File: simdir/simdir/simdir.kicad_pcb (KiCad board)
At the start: 2 copper layers, 5 parts, among them U2 MASWSS0178, U3 MASWSS0178, U4 MASWSS0178, U5 MASWSS0178, U6 MASWSS0178

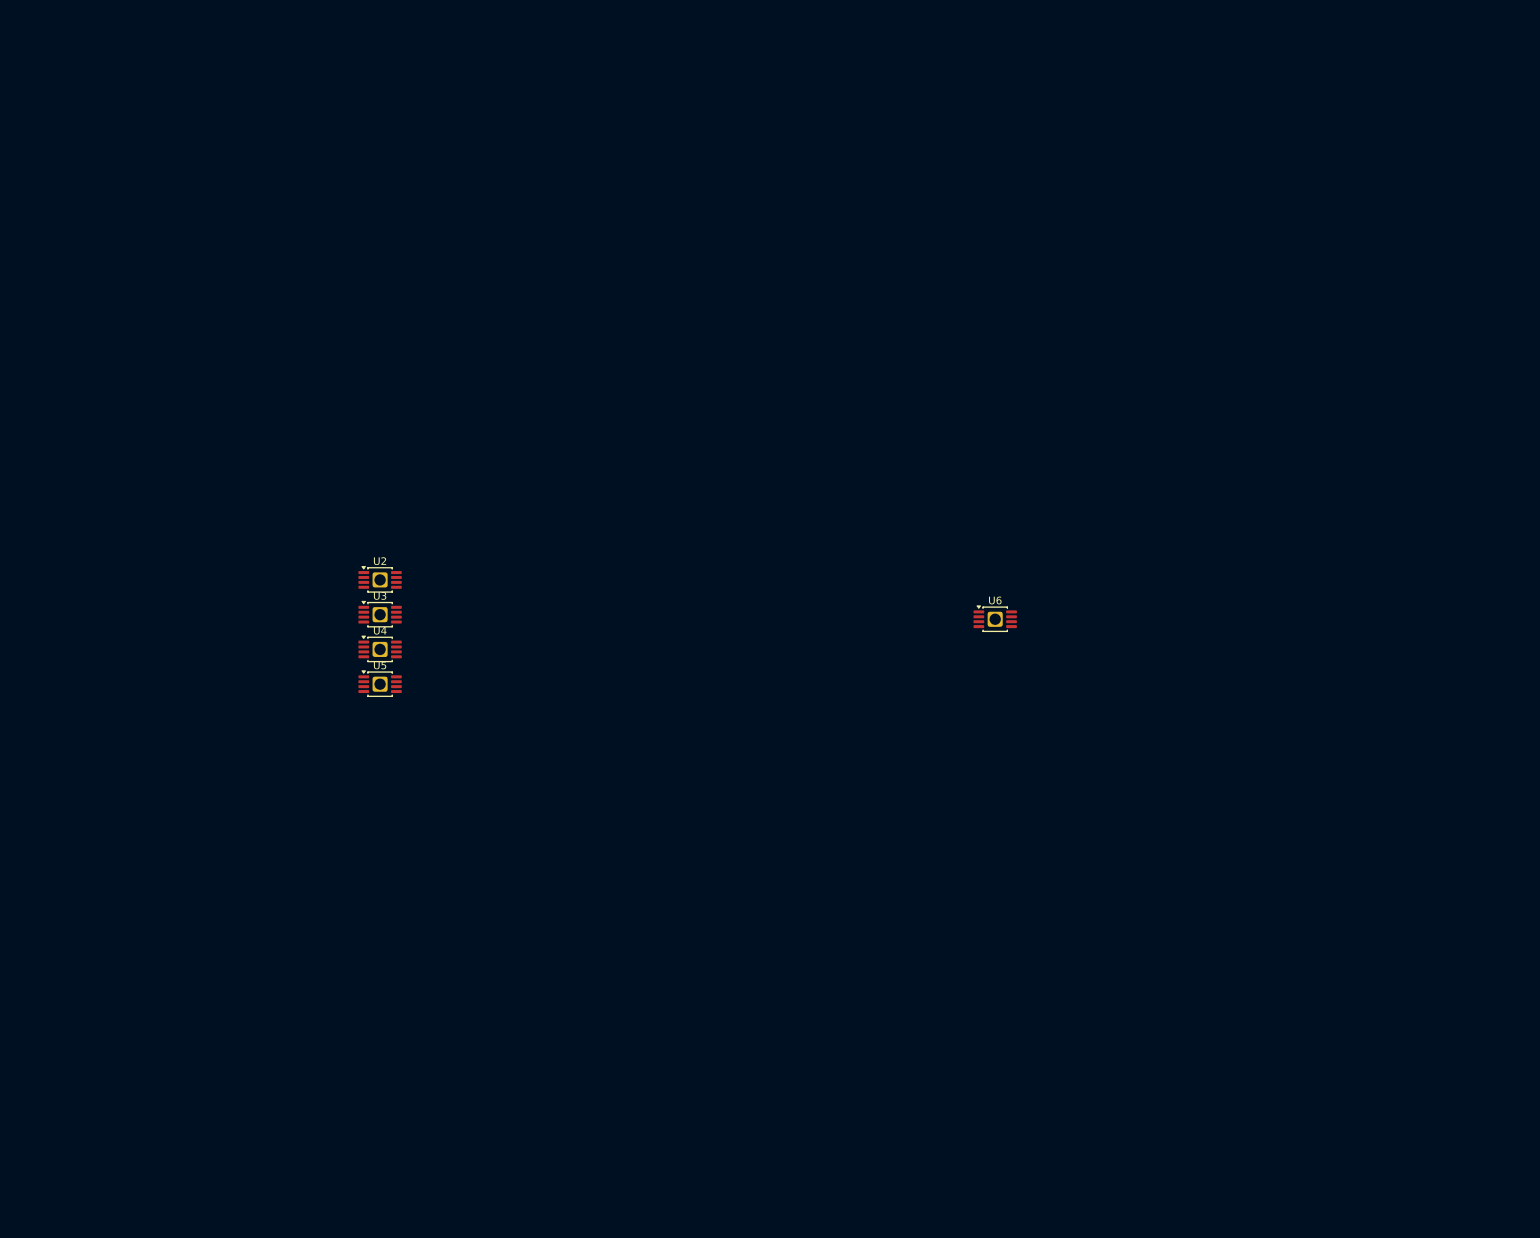
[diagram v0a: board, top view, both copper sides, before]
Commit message: Added channel block.
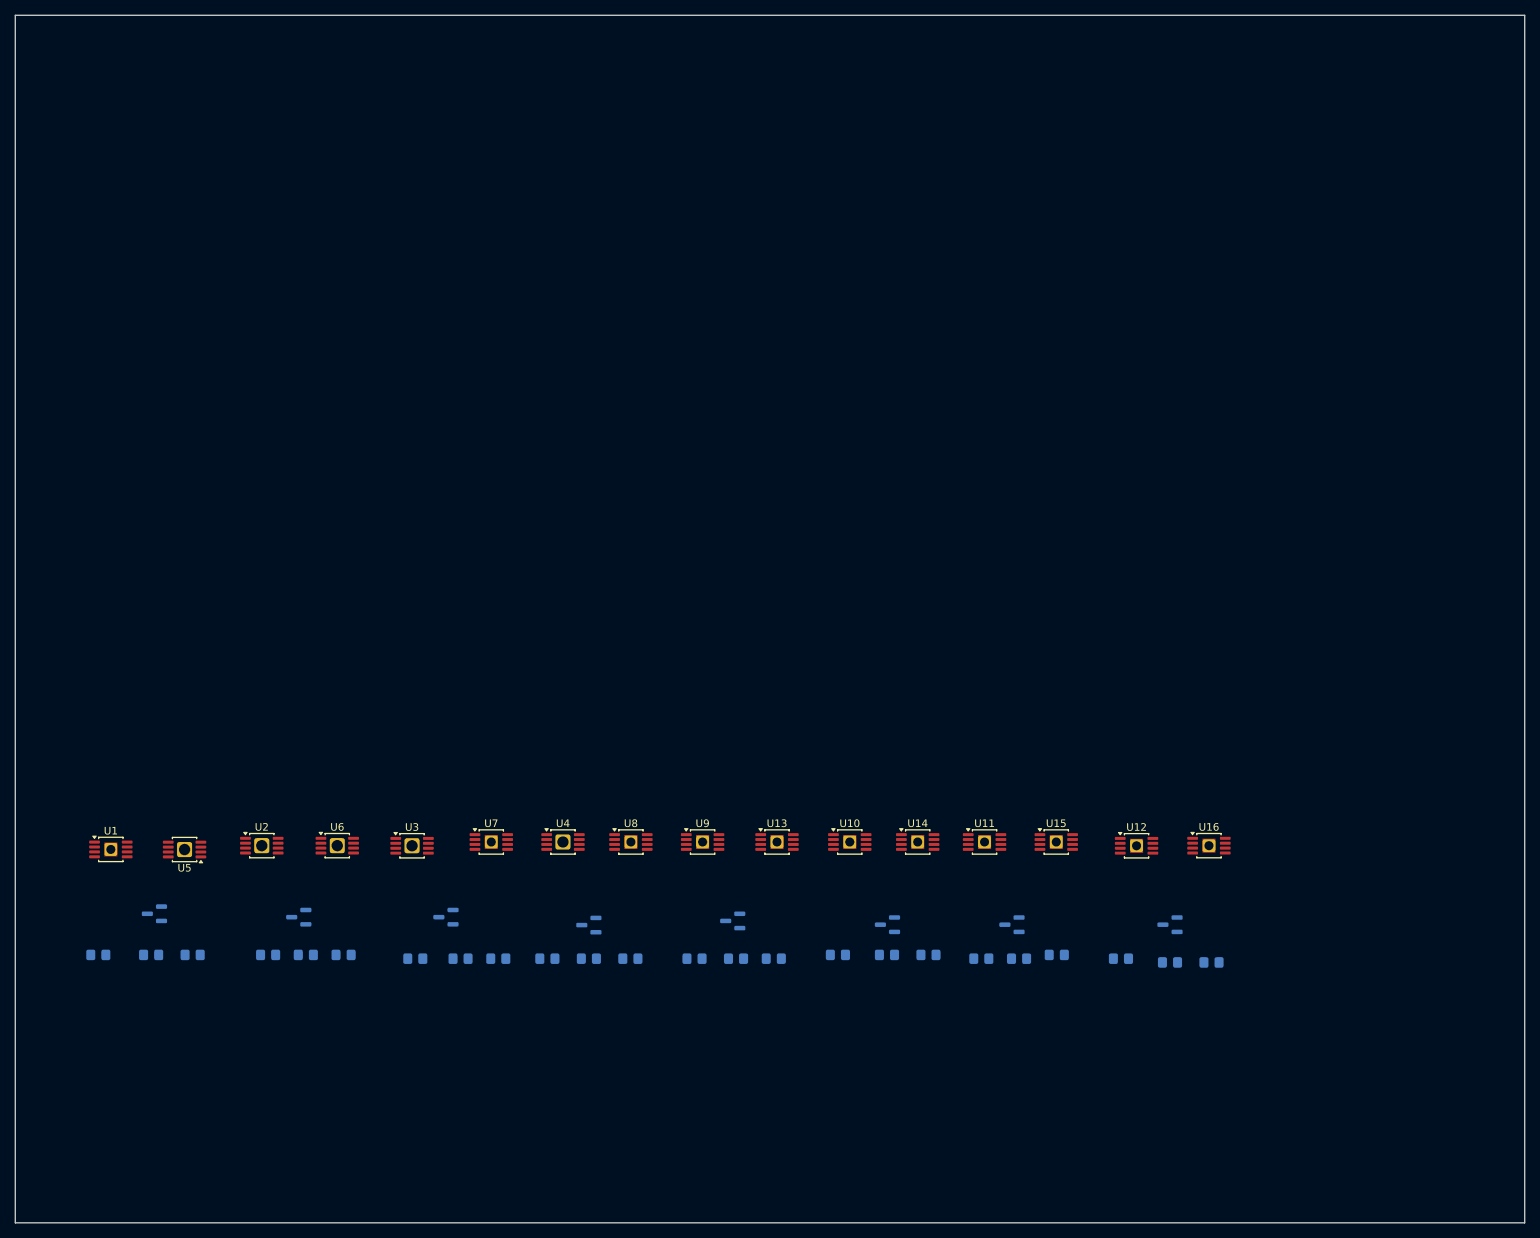
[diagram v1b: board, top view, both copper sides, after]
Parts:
- added Q1: BC847, Package_TO_SOT_SMD:SOT-23, B.Cu at (38.4, 139.1)
- added Q2: BC847, Package_TO_SOT_SMD:SOT-23, B.Cu at (57.6, 139.5)
- added Q3: BC847, Package_TO_SOT_SMD:SOT-23, B.Cu at (77.1, 139.5)
- added Q4: BC847, Package_TO_SOT_SMD:SOT-23, B.Cu at (96.0, 140.6)
- added Q5: BC847, Package_TO_SOT_SMD:SOT-23, B.Cu at (115.1, 140.0)
- added Q6: BC847, Package_TO_SOT_SMD:SOT-23, B.Cu at (135.6, 140.5)
- added Q7: BC847, Package_TO_SOT_SMD:SOT-23, B.Cu at (152.1, 140.5)
- added Q8: BC847, Package_TO_SOT_SMD:SOT-23, B.Cu at (173.0, 140.5)
- added R1: 10k, Resistor_SMD:R_0805_2012Metric_Pad1.20x1.40mm_HandSolder, B.Cu at (31.0, 144.5)
- added R10: 10k, Resistor_SMD:R_0805_2012Metric_Pad1.20x1.40mm_HandSolder, B.Cu at (90.5, 145.0)
- added R11: 4.7k, Resistor_SMD:R_0805_2012Metric_Pad1.20x1.40mm_HandSolder, B.Cu at (96.0, 145.0)
- added R12: 10k, Resistor_SMD:R_0805_2012Metric_Pad1.20x1.40mm_HandSolder, B.Cu at (101.5, 145.0)
- added R13: 10k, Resistor_SMD:R_0805_2012Metric_Pad1.20x1.40mm_HandSolder, B.Cu at (110.0, 145.0)
- added R14: 4.7k, Resistor_SMD:R_0805_2012Metric_Pad1.20x1.40mm_HandSolder, B.Cu at (115.5, 145.0)
- added R15: 10k, Resistor_SMD:R_0805_2012Metric_Pad1.20x1.40mm_HandSolder, B.Cu at (120.5, 145.0)
- added R16: 10k, Resistor_SMD:R_0805_2012Metric_Pad1.20x1.40mm_HandSolder, B.Cu at (129.0, 144.5)
- added R17: 4.7k, Resistor_SMD:R_0805_2012Metric_Pad1.20x1.40mm_HandSolder, B.Cu at (135.5, 144.5)
- added R18: 10k, Resistor_SMD:R_0805_2012Metric_Pad1.20x1.40mm_HandSolder, B.Cu at (141.0, 144.5)
- added R19: 10k, Resistor_SMD:R_0805_2012Metric_Pad1.20x1.40mm_HandSolder, B.Cu at (148.0, 145.0)
- added R2: 10k, Resistor_SMD:R_0805_2012Metric_Pad1.20x1.40mm_HandSolder, B.Cu at (38.0, 144.5)
- added R20: 4.7k, Resistor_SMD:R_0805_2012Metric_Pad1.20x1.40mm_HandSolder, B.Cu at (153.0, 145.0)
- added R21: 10k, Resistor_SMD:R_0805_2012Metric_Pad1.20x1.40mm_HandSolder, B.Cu at (158.0, 144.5)
- added R22: 10k, Resistor_SMD:R_0805_2012Metric_Pad1.20x1.40mm_HandSolder, B.Cu at (166.5, 145.0)
- added R23: 4.7k, Resistor_SMD:R_0805_2012Metric_Pad1.20x1.40mm_HandSolder, B.Cu at (173.0, 145.5)
- added R24: 10k, Resistor_SMD:R_0805_2012Metric_Pad1.20x1.40mm_HandSolder, B.Cu at (178.5, 145.5)
- added R3: 4.7k, Resistor_SMD:R_0805_2012Metric_Pad1.20x1.40mm_HandSolder, B.Cu at (43.5, 144.5)
- added R4: 10k, Resistor_SMD:R_0805_2012Metric_Pad1.20x1.40mm_HandSolder, B.Cu at (53.5, 144.5)
- added R5: 4.7k, Resistor_SMD:R_0805_2012Metric_Pad1.20x1.40mm_HandSolder, B.Cu at (58.5, 144.5)
- added R6: 10k, Resistor_SMD:R_0805_2012Metric_Pad1.20x1.40mm_HandSolder, B.Cu at (63.5, 144.5)
- added R7: 10k, Resistor_SMD:R_0805_2012Metric_Pad1.20x1.40mm_HandSolder, B.Cu at (73.0, 145.0)
- added R8: 4.7k, Resistor_SMD:R_0805_2012Metric_Pad1.20x1.40mm_HandSolder, B.Cu at (79.0, 145.0)
- added R9: 10k, Resistor_SMD:R_0805_2012Metric_Pad1.20x1.40mm_HandSolder, B.Cu at (84.0, 145.0)
- added U1: MASWSS0178, hand:MSOP-8-1EP_3x3mm_P0.65mm_EP1.73x1.85mm_hand, F.Cu at (32.7, 130.5)
- added U10: MASWSS0178, hand:MSOP-8-1EP_3x3mm_P0.65mm_EP1.73x1.85mm_hand, F.Cu at (130.6, 129.5)
- added U11: MASWSS0178, hand:MSOP-8-1EP_3x3mm_P0.65mm_EP1.73x1.85mm_hand, F.Cu at (148.4, 129.5)
- added U12: MASWSS0178, hand:MSOP-8-1EP_3x3mm_P0.65mm_EP1.73x1.85mm_hand, F.Cu at (168.6, 130.0)
- added U13: MASWSS0178, hand:MSOP-8-1EP_3x3mm_P0.65mm_EP1.73x1.85mm_hand, F.Cu at (120.9, 129.5)
- added U14: MASWSS0178, hand:MSOP-8-1EP_3x3mm_P0.65mm_EP1.73x1.85mm_hand, F.Cu at (139.6, 129.5)
- added U15: MASWSS0178, hand:MSOP-8-1EP_3x3mm_P0.65mm_EP1.73x1.85mm_hand, F.Cu at (157.9, 129.5)
- added U16: MASWSS0178, hand:MSOP-8-1EP_3x3mm_P0.65mm_EP1.73x1.85mm_hand, F.Cu at (178.2, 130.0)
- added U7: MASWSS0178, hand:MSOP-8-1EP_3x3mm_P0.65mm_EP1.73x1.85mm_hand, F.Cu at (83.1, 129.5)
- added U8: MASWSS0178, hand:MSOP-8-1EP_3x3mm_P0.65mm_EP1.73x1.85mm_hand, F.Cu at (101.6, 129.5)
- added U9: MASWSS0178, hand:MSOP-8-1EP_3x3mm_P0.65mm_EP1.73x1.85mm_hand, F.Cu at (111.1, 129.5)
- moved U6 92.2 mm to (62.7, 130.0)
- moved U2 38.5 mm to (52.7, 130.0)
- moved U4 35.2 mm to (92.6, 129.5)
- moved U5 33.9 mm to (42.4, 130.5), turned to 180 degrees
- moved U3 30.9 mm to (72.6, 130.0)
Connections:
- U2 pad 1: unconnected-(U2-CTL1-Pad1) -> Net-(U2-CTL1)
- U2 pad 2: unconnected-(U2-CTL2-Pad2) -> Net-(Q2-C)
- U2 pad 3: unconnected-(U2-RFC-Pad3) -> Net-(U2-RFC)
- U2 pad 4: Net-(U2-GND-Pad4) -> /channel1/GND
- U2 pad 5: unconnected-(U2-RF2-Pad5) -> Net-(U2-RF2)
- U2 pad 6: Net-(U2-GND-Pad4) -> /channel1/GND
- U2 pad 7: Net-(U2-GND-Pad4) -> /channel1/GND
- U2 pad 8: unconnected-(U2-RF1-Pad8) -> Net-(U2-RF1)
- U2 pad 9: Net-(U2-GND-Pad4) -> /channel1/GND
- U3 pad 1: unconnected-(U3-CTL1-Pad1) -> Net-(U3-CTL1)
- U3 pad 2: unconnected-(U3-CTL2-Pad2) -> Net-(Q3-C)
- U3 pad 3: unconnected-(U3-RFC-Pad3) -> Net-(U3-RFC)
- U3 pad 4: Net-(U3-GND-Pad4) -> /channel1/GND
- U3 pad 5: unconnected-(U3-RF2-Pad5) -> Net-(U3-RF2)
- U3 pad 6: Net-(U3-GND-Pad4) -> /channel1/GND
- U3 pad 7: Net-(U3-GND-Pad4) -> /channel1/GND
- U3 pad 8: unconnected-(U3-RF1-Pad8) -> Net-(U3-RF1)
- U3 pad 9: Net-(U3-GND-Pad4) -> /channel1/GND
- U4 pad 1: unconnected-(U4-CTL1-Pad1) -> Net-(U4-CTL1)
- U4 pad 2: unconnected-(U4-CTL2-Pad2) -> Net-(Q4-C)
- U4 pad 3: unconnected-(U4-RFC-Pad3) -> Net-(U4-RFC)
- U4 pad 4: Net-(U4-GND-Pad4) -> /channel1/GND
- U4 pad 5: unconnected-(U4-RF2-Pad5) -> Net-(U4-RF2)
- U4 pad 6: Net-(U4-GND-Pad4) -> /channel1/GND
- U4 pad 7: Net-(U4-GND-Pad4) -> /channel1/GND
- U4 pad 8: unconnected-(U4-RF1-Pad8) -> Net-(U4-RF1)
- U4 pad 9: Net-(U4-GND-Pad4) -> /channel1/GND
- U5 pad 1: unconnected-(U5-CTL1-Pad1) -> Net-(Q1-C)
- U5 pad 2: unconnected-(U5-CTL2-Pad2) -> Net-(U1-CTL1)
- U5 pad 3: unconnected-(U5-RFC-Pad3) -> Net-(U2-RFC)
- U5 pad 4: Net-(U5-GND-Pad4) -> /channel1/GND
- U5 pad 5: unconnected-(U5-RF2-Pad5) -> Net-(U1-RF1)
- U5 pad 6: Net-(U5-GND-Pad4) -> /channel1/GND
- U5 pad 7: Net-(U5-GND-Pad4) -> /channel1/GND
- U5 pad 8: unconnected-(U5-RF1-Pad8) -> Net-(U1-RF2)
- U5 pad 9: Net-(U5-GND-Pad4) -> /channel1/GND
- U6 pad 1: unconnected-(U6-CTL1-Pad1) -> Net-(Q2-C)
- U6 pad 2: unconnected-(U6-CTL2-Pad2) -> Net-(U2-CTL1)
- U6 pad 3: unconnected-(U6-RFC-Pad3) -> Net-(U3-RFC)
- U6 pad 4: Net-(U6-GND-Pad4) -> /channel1/GND
- U6 pad 5: unconnected-(U6-RF2-Pad5) -> Net-(U2-RF1)
- U6 pad 6: Net-(U6-GND-Pad4) -> /channel1/GND
- U6 pad 7: Net-(U6-GND-Pad4) -> /channel1/GND
- U6 pad 8: unconnected-(U6-RF1-Pad8) -> Net-(U2-RF2)
- U6 pad 9: Net-(U6-GND-Pad4) -> /channel1/GND
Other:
- board outline added: 200 x 160 mm
- copper layers 2 -> 4

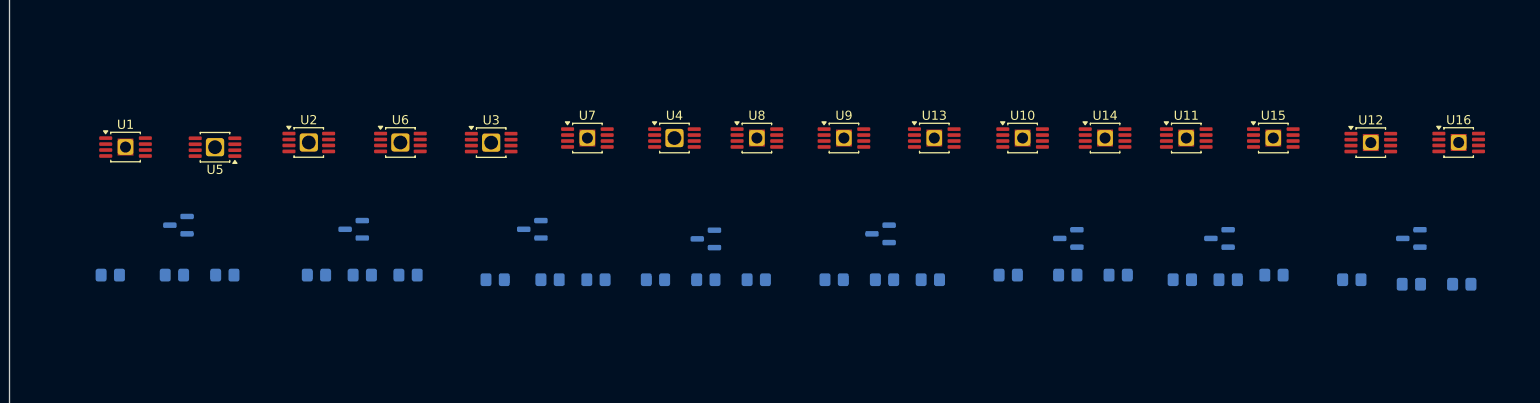
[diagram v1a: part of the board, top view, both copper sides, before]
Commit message: Update component spacing.
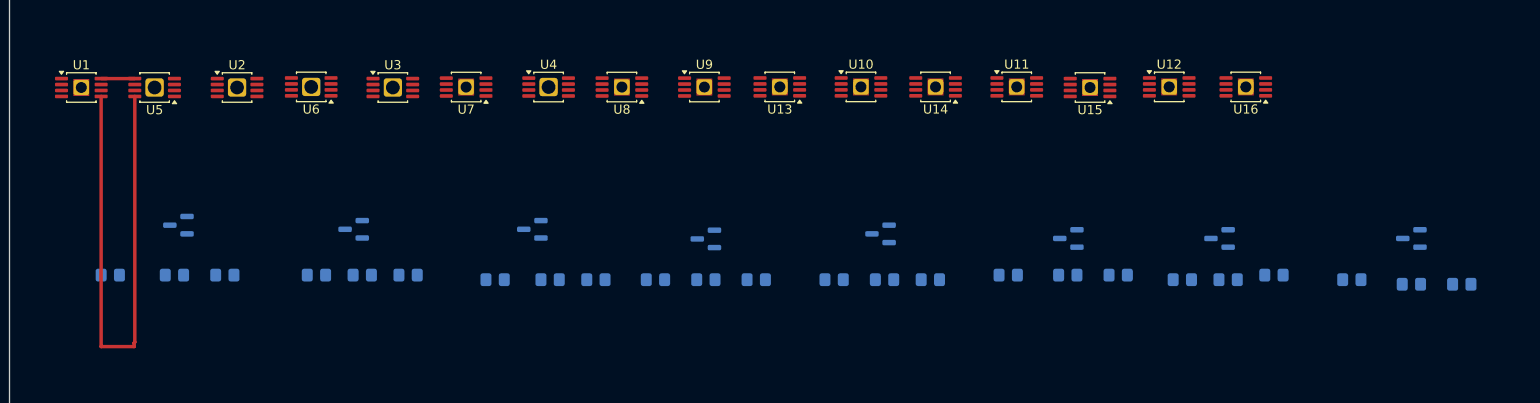
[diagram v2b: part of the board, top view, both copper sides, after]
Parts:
- moved U16 24.0 mm to (154.9, 124.0), turned to 180 degrees
- moved U12 22.8 mm to (146.6, 124.0)
- moved U15 20.7 mm to (137.9, 124.0), turned to 180 degrees
- moved U11 19.3 mm to (129.9, 124.0)
- moved U14 19.3 mm to (121.1, 124.0), turned to 180 degrees
- moved U10 18.5 mm to (112.9, 124.0)
- moved U13 17.8 mm to (104.1, 124.0), turned to 180 degrees
- moved U9 16.2 mm to (95.8, 124.0)
- moved U8 15.7 mm to (86.8, 124.0), turned to 180 degrees
- moved U4 14.8 mm to (78.8, 124.0)
- moved U7 14.4 mm to (69.8, 124.0), turned to 180 degrees
- moved U3 12.3 mm to (61.8, 124.0)
- moved U6 11.5 mm to (52.9, 124.0), turned to 180 degrees
- moved U2 9.86 mm to (44.8, 124.0)
- moved U5 9.27 mm to (35.8, 124.0)
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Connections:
- net Net-(U1-RF1) renamed /channel1/RF0_ref
- net Net-(U1-RF2) renamed /channel1/RF0_meander
- net Net-(U10-RF1) renamed /channel1/RF5_ref
- net Net-(U10-RF2) renamed /channel1/RF5_meander
- net Net-(U11-RF1) renamed /channel1/RF6_ref
- net Net-(U11-RF2) renamed /channel1/RF6_meander
- net Net-(U12-RF1) renamed /channel1/RF7_ref
- net Net-(U12-RF2) renamed /channel1/RF7_meander
- net Net-(U13-RF1) renamed /channel1/RF4_meander
- net Net-(U13-RF2) renamed /channel1/RF4_ref
- net Net-(U2-RF1) renamed /channel1/RF1_ref
- net Net-(U2-RF2) renamed /channel1/RF1_meander
- net Net-(U3-RF1) renamed /channel1/RF2_ref
- net Net-(U3-RF2) renamed /channel1/RF2_meander
- net Net-(U4-RF2) renamed /channel1/RF3_meander
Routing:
- net /channel1/RF0_meander: track 0.00 -> 58.2 mm
- net /channel1/RF0_ref: track 0.00 -> 3.67 mm

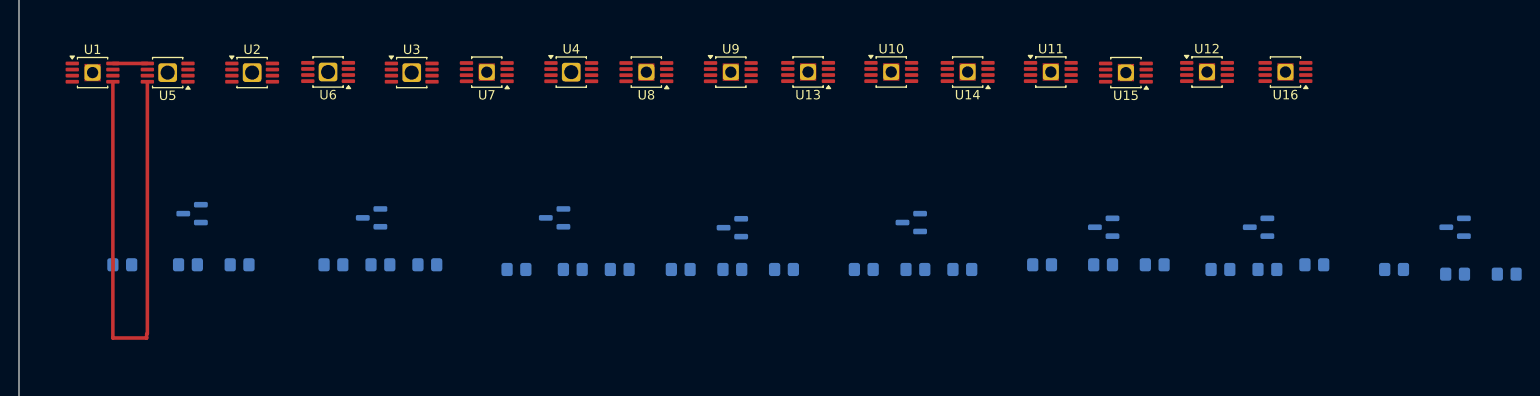
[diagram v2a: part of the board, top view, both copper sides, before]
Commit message: Added meanders for 6 & 7.
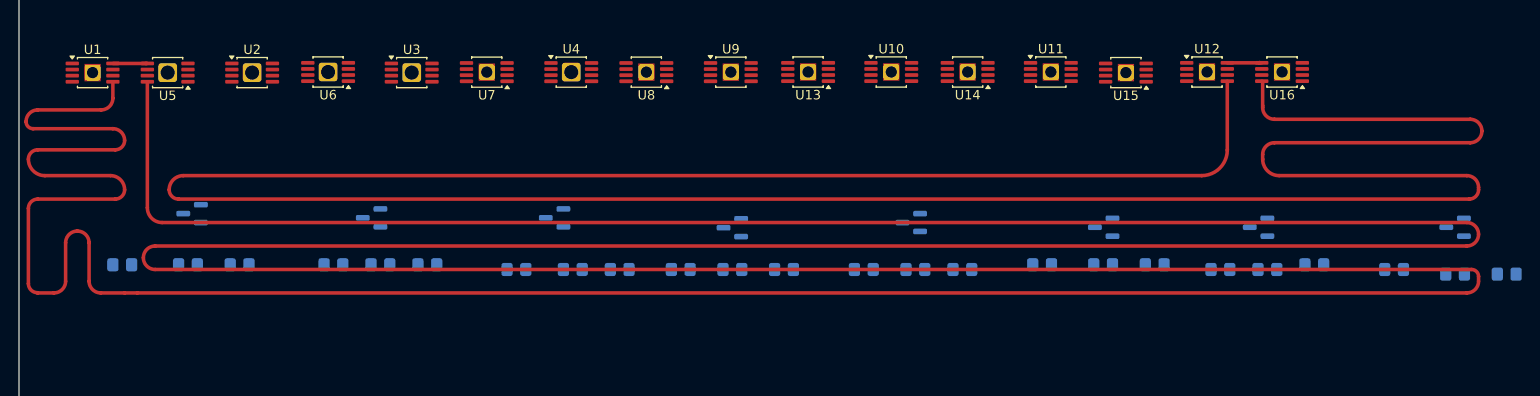
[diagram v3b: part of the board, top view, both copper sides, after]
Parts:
- moved U16 0.37 mm to (154.6, 124.0)
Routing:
- net /channel1/RF0_meander: track 58.2 -> 677.2 mm
- net /channel1/RF7_meander: track 0.00 -> 340.4 mm
- net /channel1/RF7_ref: track 0.00 -> 3.72 mm
